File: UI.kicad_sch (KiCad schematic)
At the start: 8 parts, among them SW501 SW_Push, SW502 SW_Push

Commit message: Rename and update layout
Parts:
- removed C501, C502: 100nF/50V, Capacitor_SMD:C_0603_1608Metric, symbol Device:C_Small
- removed SW501, SW502: SW_Push, Button_Switch_SMD:SW_SPST_TL3342, symbol Switch:SW_Push
- added C801: 100nF, Capacitor_SMD:C_0402_1005Metric, symbol Device:C
- added D801: YELLOW LED, LED_SMD:LED_0603_1608Metric, symbol Device:LED
- added R801: 2k, Resistor_SMD:R_0402_1005Metric, symbol Device:R
- added U801: AH1902, Package_TO_SOT_SMD:SOT-553, symbol SH-ESP32-mini:AH1902
- renumbered D501 to D802, D502 to D803, R501 to R802, R502 to R803
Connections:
- net +3V3: now also C801.2, U801.4 (Vdd)
- net GND: now also C801.1, D801.1 (K), U801.2 (GND)
- net LED renamed BLUE_LED
- new net: D801.2 (A), R801.2
- new net HALL_OUTPUT: U801.5 (OUTPUT)
- new net YELLOW_LED: R801.1
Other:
- note added: "AH1902 hall effect sensor for contactless reset functionality"
- note removed: "Boot"
- note removed: "Reset"
- title: Sailor Hat with ESP32 -> SH-wg

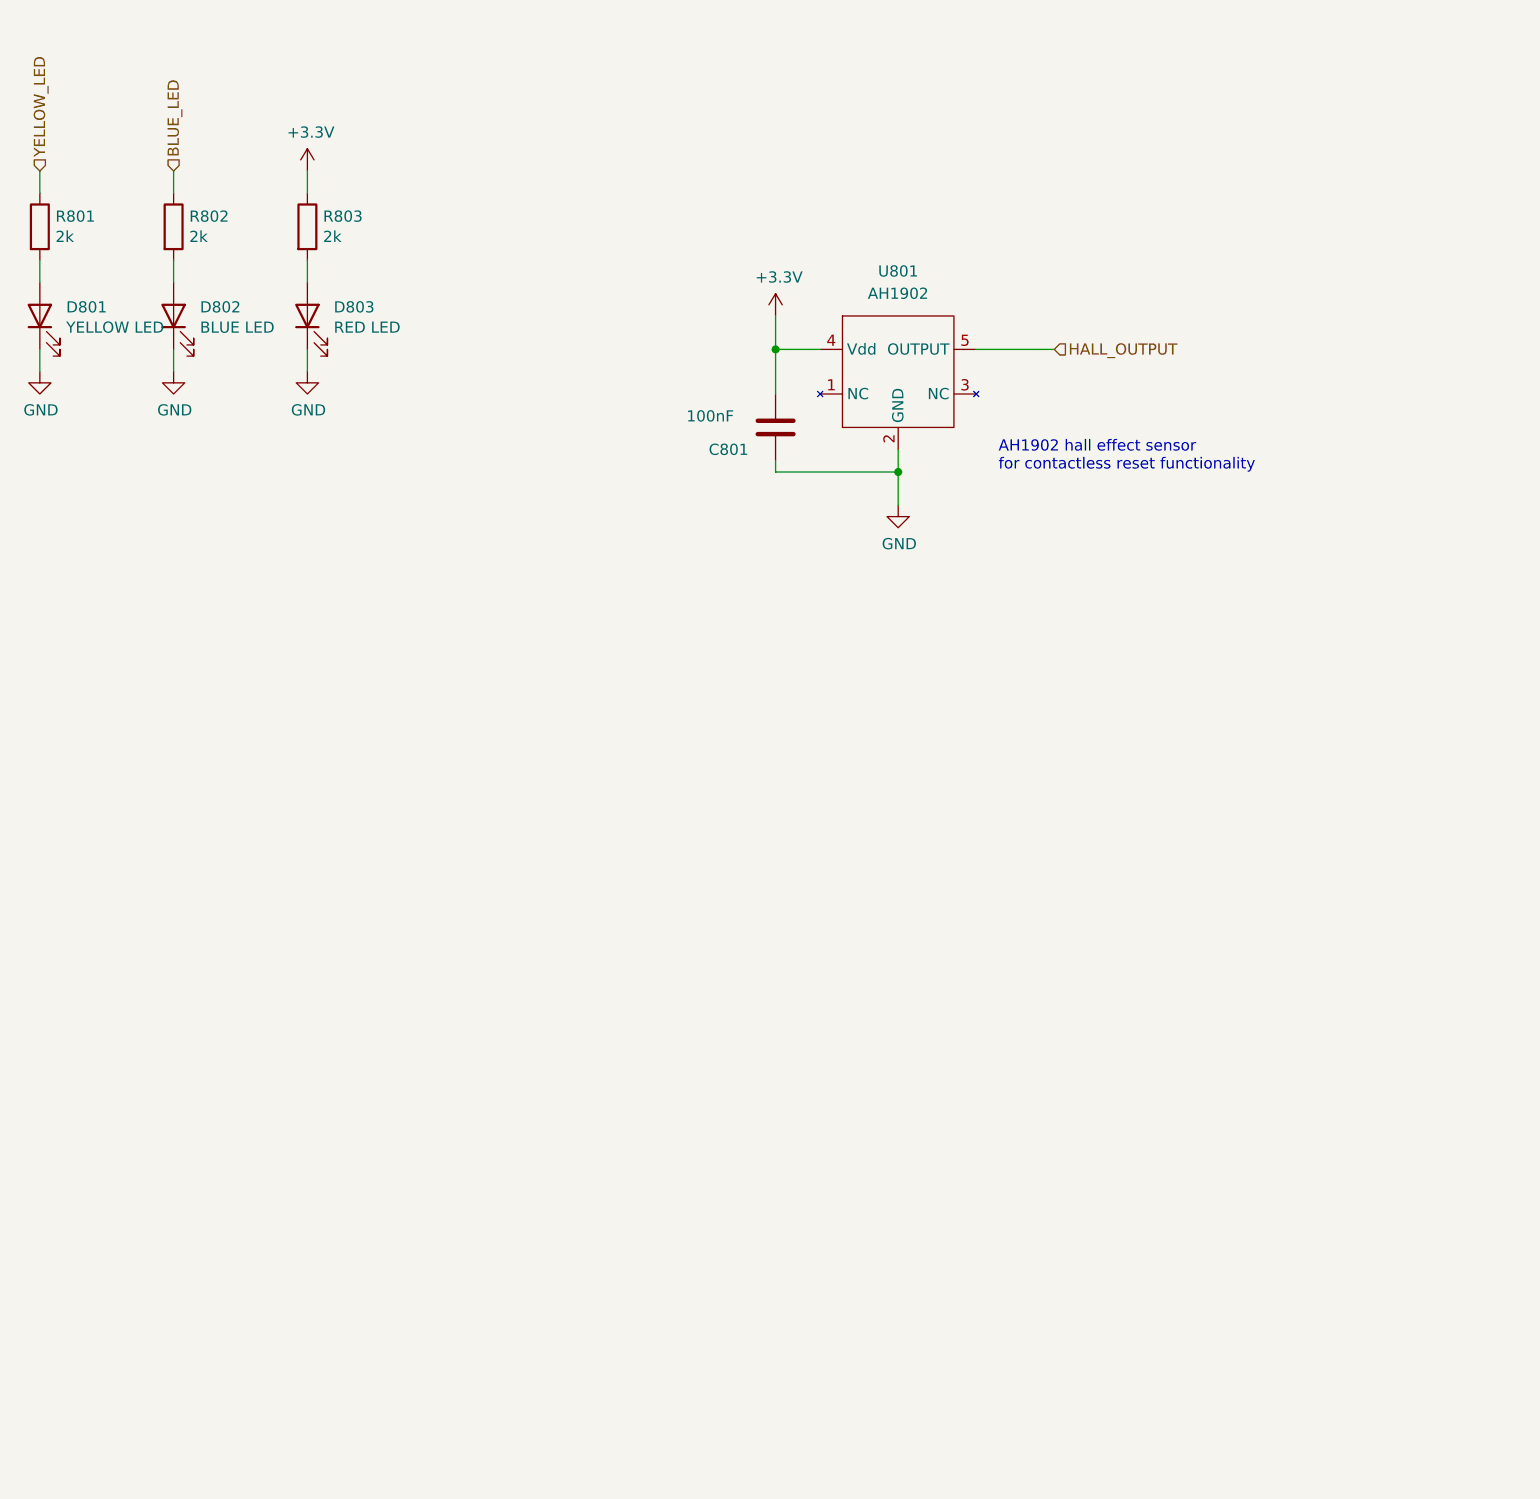
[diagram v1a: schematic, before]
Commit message: Add headers & LEDs
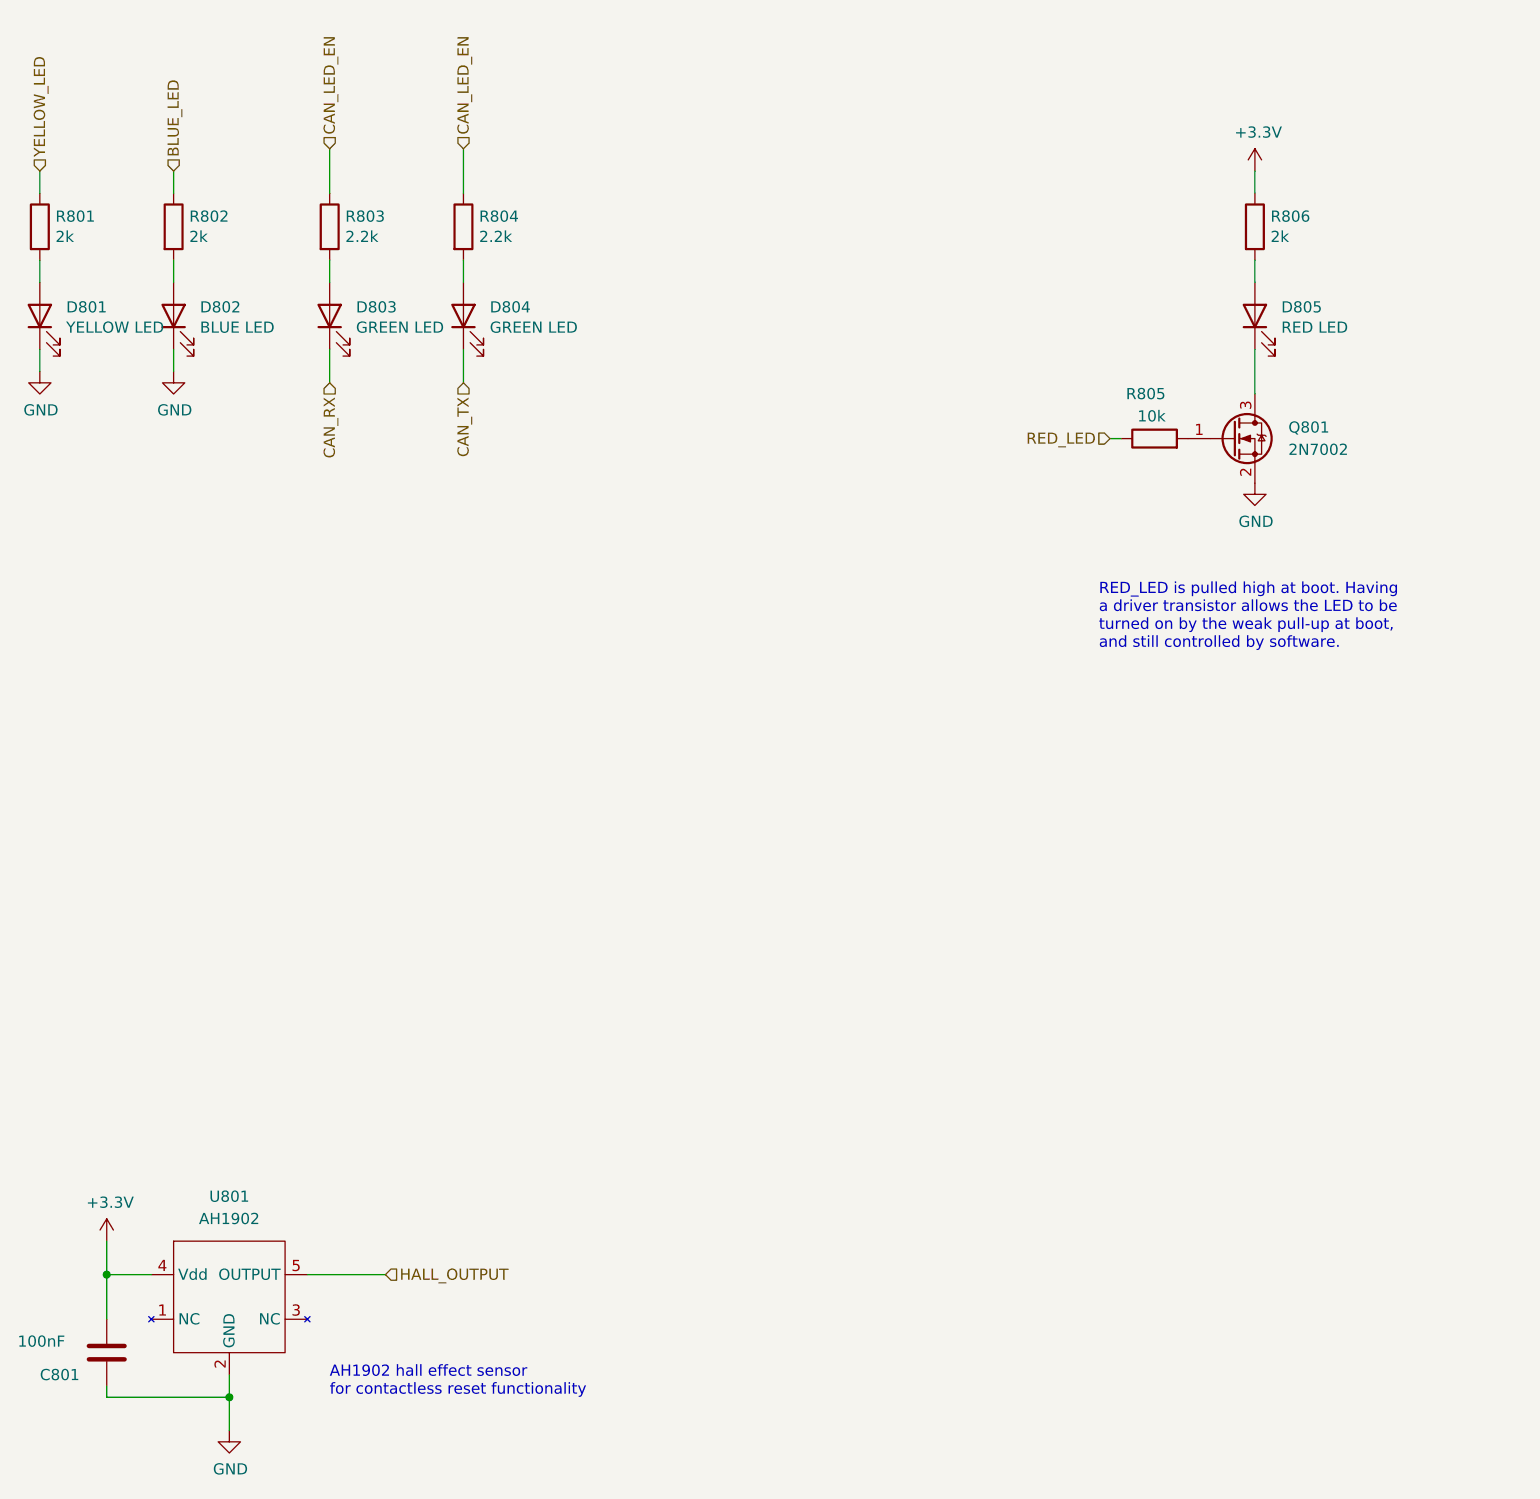
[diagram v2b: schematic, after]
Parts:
- added D803, D804: GREEN LED, LED_SMD:LED_0603_1608Metric, symbol Device:LED
- added Q801: 2N7002, Package_TO_SOT_SMD:SOT-23, symbol Transistor_FET:2N7002
- added R803, R804: 2.2k, Resistor_SMD:R_0402_1005Metric, symbol Device:R
- added R805: 10k, Resistor_SMD:R_0402_1005Metric, symbol Device:R
- renumbered D803 to D805, R803 to R806
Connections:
- net GND: now also Q801.2 (S); no longer D805.1 (K)
- new net: D805.1 (K), Q801.3 (D)
- new net: D804.2 (A), R804.2
- new net: D803.2 (A), R803.2
- new net: Q801.1 (G), R805.2
- new net CAN_LED_EN: R803.1, R804.1
- new net CAN_RX: D803.1 (K)
- new net CAN_TX: D804.1 (K)
- new net RED_LED: R805.1
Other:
- note added: "RED_LED is pulled high at boot. Having a driver transistor allows the LED to be turned on by the weak pull-up at boot, and still controlled by software."
- moved on the sheet: C801, D805, R806, U801

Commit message: Finish 0.1.0 design
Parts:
- D801: LCSC (none) -> C72038
- R802: value 2k -> 1.5k; LCSC C4109 -> C25867
- R803, R804: value 2.2k -> 2k; LCSC C25879 -> C4109
- R805: LCSC (none) -> C25744
- R806: value 2k -> 2.2k; LCSC C4109 -> C25879
- U801: symbol SH-ESP32-mini:AH1902 -> SH-wg:AH1902
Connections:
- net HALL_OUTPUT renamed HALL
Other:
- note added: "RED_LED is pulled high at boot. Having a driver transistor allows the LED to be turned on by the weak pull-up at boot, and still be controlled by software."
- note removed: "RED_LED is pulled high at boot. Having a driver transistor allows the LED to be turned on by the weak pull-up at boot, and still controlled by software."
- title: SH-wg -> Sailor Hat WiFi Gateway
- moved on the sheet: D803, D804

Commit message: Prepare final 0.1.0 proto
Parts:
- U801: LCSC (none) -> C239188
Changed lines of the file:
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@@
+      (effects (font (size 1.27 1.27)) hide)
+    )
+    (property "LCSC" "C239188" (id 4) (at 50.8 158.75 0)
       (effects (font (size 1.27 1.27)) hide)
     )

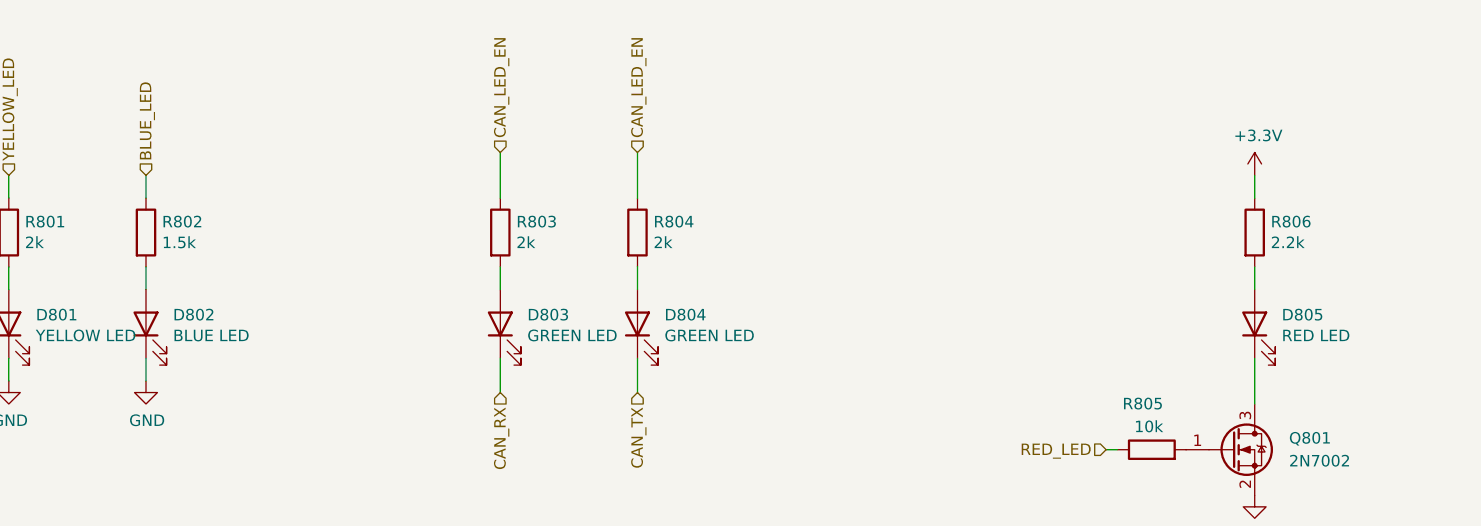
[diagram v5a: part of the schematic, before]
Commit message: Update LED resistor values, improve PCB edge clearance
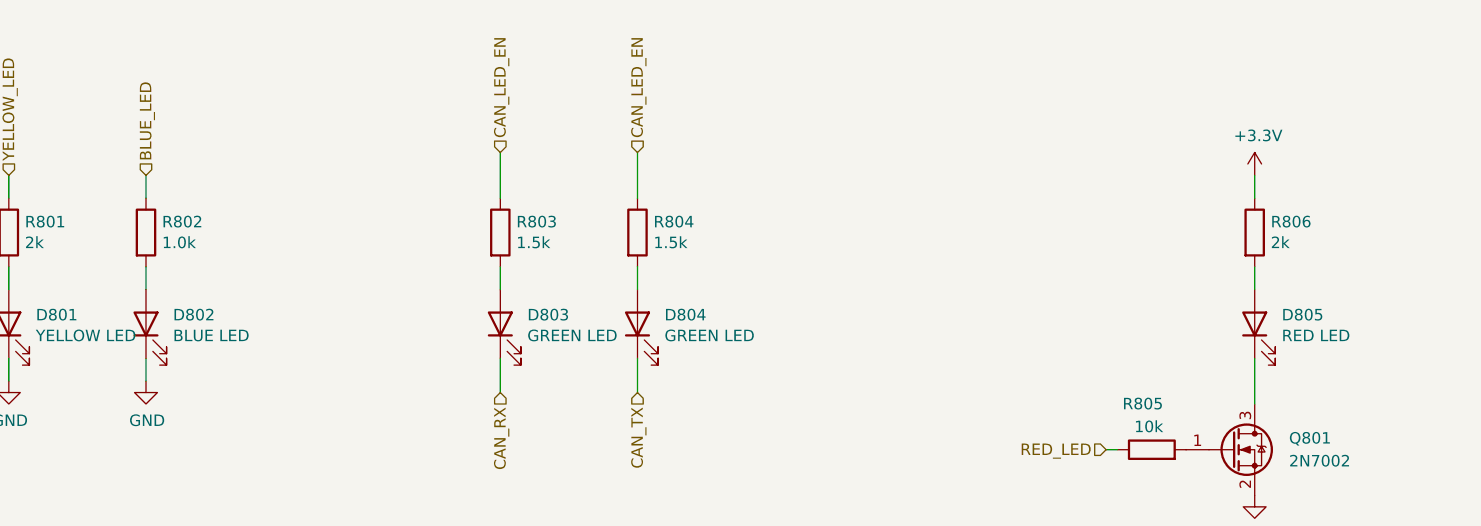
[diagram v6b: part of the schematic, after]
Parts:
- R802: value 1.5k -> 1.0k; LCSC C25867 -> C11702
- R803, R804: value 2k -> 1.5k; LCSC C4109 -> C25867
- R806: value 2.2k -> 2k; LCSC C25879 -> C4109
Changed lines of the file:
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@@
       (effects (font (size 1.27 1.27)) (justify left))
     )
-    (property "Value" "1.5k" (id 1) (at 46.228 37.973 0)
+    (property "Value" "1.0k" (id 1) (at 46.228 37.973 0)
       (effects (font (size 1.27 1.27)) (justify left))
     )
@@
       (effects (font (size 1.27 1.27)) hide)
     )
-    (property "LCSC" "C25867" (id 4) (at 44.45 36.83 0)
+    (property "LCSC" "C11702" (id 4) (at 44.45 36.83 0)
       (effects (font (size 1.27 1.27)) hide)
     )
@@
       (effects (font (size 1.27 1.27)) (justify left))
     )
-    (property "Value" "2k" (id 1) (at 100.838 37.973 0)
+    (property "Value" "1.5k" (id 1) (at 100.838 37.973 0)
       (effects (font (size 1.27 1.27)) (justify left))
     )
@@
       (effects (font (size 1.27 1.27)) hide)
     )
-    (property "LCSC" "C4109" (id 4) (at 99.06 36.83 0)
+    (property "LCSC" "C25867" (id 4) (at 99.06 36.83 0)
       (effects (font (size 1.27 1.27)) hide)
     )
@@
       (effects (font (size 1.27 1.27)) (justify left))
     )
-    (property "Value" "2.2k" (id 1) (at 169.418 37.973 0)
+    (property "Value" "2k" (id 1) (at 169.418 37.973 0)
       (effects (font (size 1.27 1.27)) (justify left))
     )
@@
       (effects (font (size 1.27 1.27)) hide)
     )
-    (property "LCSC" "C25879" (id 4) (at 167.64 36.83 0)
+    (property "LCSC" "C4109" (id 4) (at 167.64 36.83 0)
       (effects (font (size 1.27 1.27)) hide)
     )
@@
       (effects (font (size 1.27 1.27)) (justify left))
     )
-    (property "Value" "2k" (id 1) (at 85.598 37.973 0)
+    (property "Value" "1.5k" (id 1) (at 85.598 37.973 0)
       (effects (font (size 1.27 1.27)) (justify left))
     )
@@
       (effects (font (size 1.27 1.27)) hide)
     )
-    (property "LCSC" "C4109" (id 4) (at 83.82 36.83 0)
-      (effects (font (size 1.27 1.27)) hide)
-    )
+    (property "LCSC" "C25867" (id 4) (at 83.82 36.83 0)
+      (effects (font (size 1.27 1.27)) hide)
+    )
